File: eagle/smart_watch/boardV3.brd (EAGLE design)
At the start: 100 x 80.3 mm, 62 parts, among them U1 MCP73831, U2 TPS61200, U3 MAX1704X, U4 V_REG_LDOSMD, Y1 16MHz

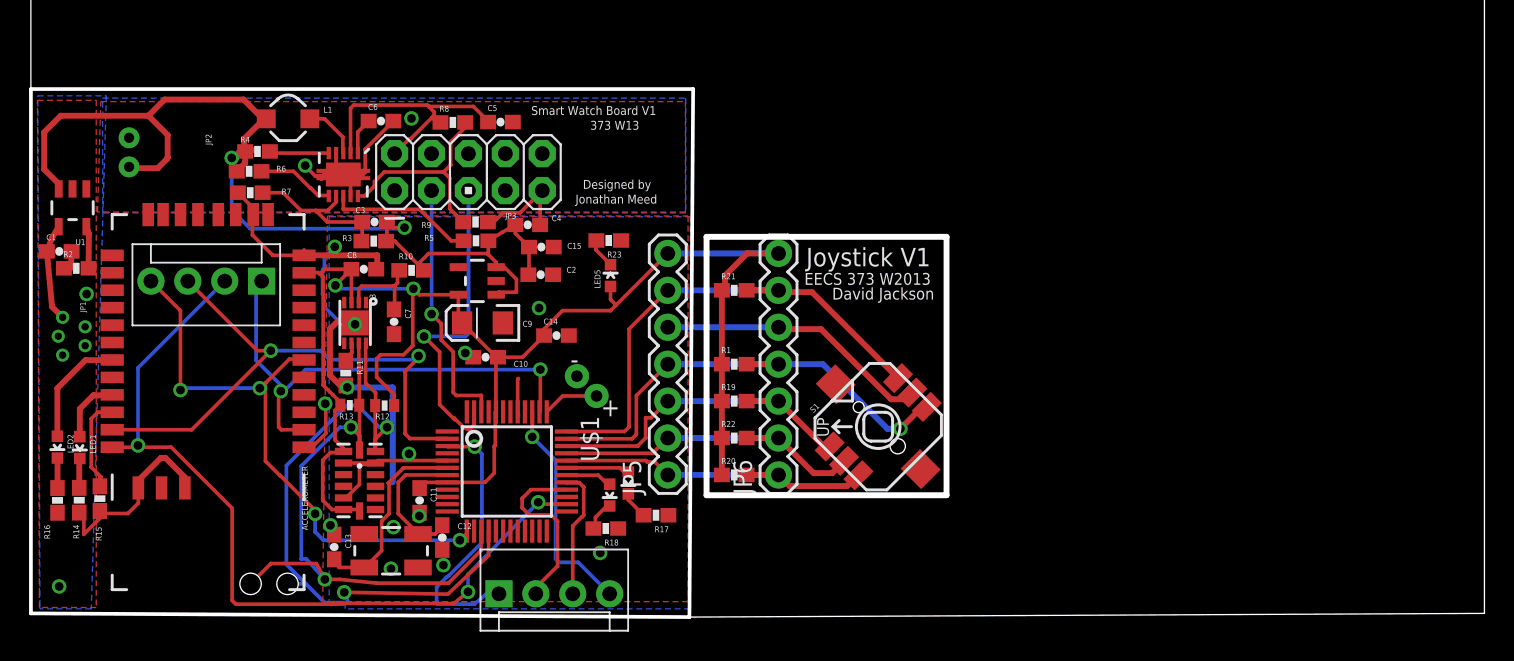
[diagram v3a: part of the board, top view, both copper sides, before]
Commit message: Updated board based on Sam's recs
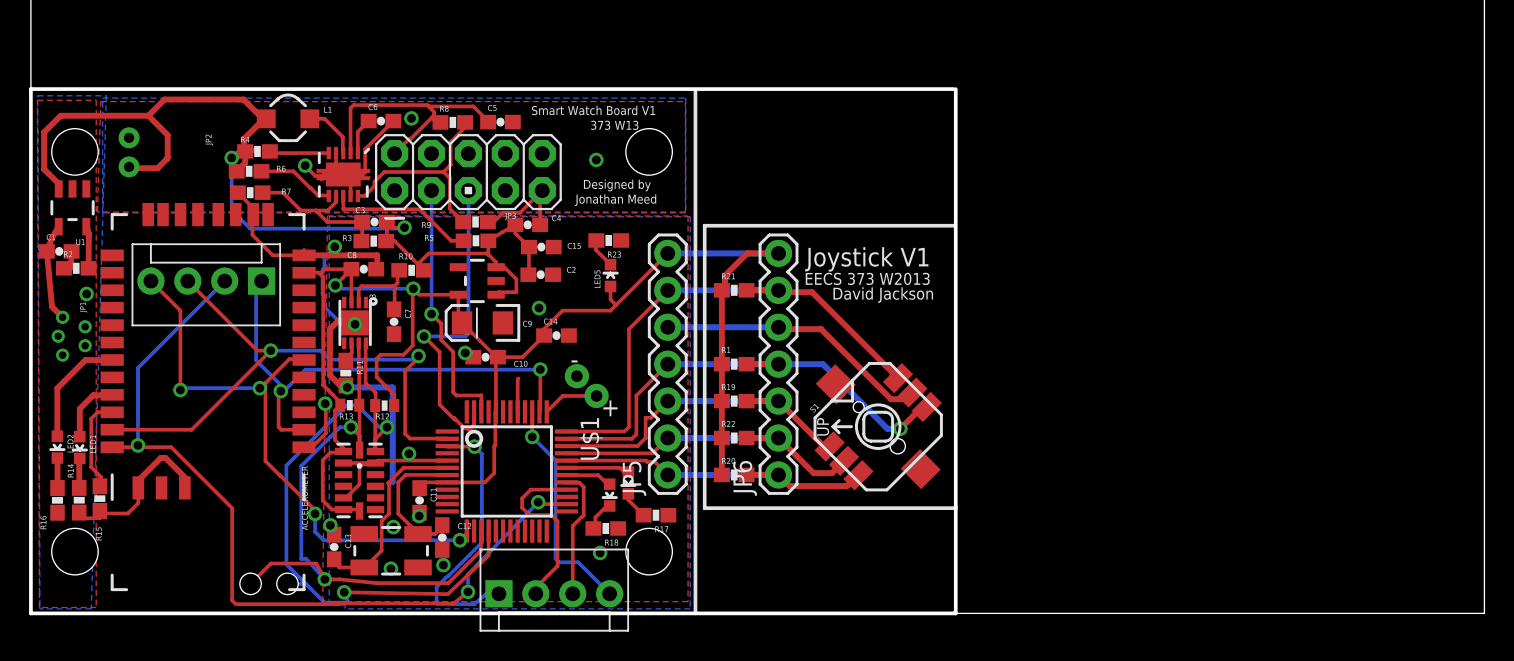
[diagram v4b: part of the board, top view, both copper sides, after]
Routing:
- net GND: track 110.6 -> 109.7 mm
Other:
- board size 100 x 80.3 mm -> 100 x 80 mm
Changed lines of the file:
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@@
 <layer number="42" name="bRestrict" color="1" fill="10" visible="no" active="yes"/>
 <layer number="43" name="vRestrict" color="2" fill="10" visible="no" active="yes"/>
-<layer number="44" name="Drills" color="7" fill="1" visible="no" active="yes"/>
-<layer number="45" name="Holes" color="7" fill="1" visible="no" active="yes"/>
+<layer number="44" name="Drills" color="7" fill="1" visible="yes" active="yes"/>
+<layer number="45" name="Holes" color="7" fill="1" visible="yes" active="yes"/>
 <layer number="46" name="Milling" color="3" fill="1" visible="no" active="yes"/>
 <layer number="47" name="Measures" color="7" fill="1" visible="no" active="yes"/>
@@
 <board>
 <plain>
-<wire x1="45.306" y1="-0.254" x2="100" y2="0" width="0" layer="20"/>
+<wire x1="63.467" y1="0" x2="63.5" y2="0" width="0" layer="20"/>
+<wire x1="63.5" y1="0" x2="100" y2="0" width="0" layer="20"/>
 <wire x1="100" y1="0" x2="100" y2="80" width="0" layer="20"/>
 <wire x1="100" y1="80" x2="0" y2="80" width="0" layer="20"/>
 <wire x1="0" y1="80" x2="0" y2="36.073615625" width="0" layer="20"/>
 <wire x1="0" y1="0" x2="0" y2="36.073615625" width="0.254" layer="20"/>
-<wire x1="45.306" y1="-0.254" x2="45.56" y2="36.073615625" width="0.254" layer="20"/>
-<wire x1="0" y1="0" x2="45.306" y2="-0.254" width="0.254" layer="20"/>
-<wire x1="0" y1="36.073615625" x2="45.56" y2="36.073615625" width="0.254" layer="20"/>
+<wire x1="0" y1="0" x2="63.467" y2="0" width="0.254" layer="20"/>
+<wire x1="0" y1="36.073615625" x2="63.467" y2="36.073615625" width="0.254" layer="20"/>
 <circle x="30.1" y="30.36" radius="1.27" width="0.254" layer="19"/>
-<circle x="3.03" y="4.25" radius="1.6" width="0.1" layer="44"/>
-<circle x="42.53" y="31.75" radius="1.6" width="0.1" layer="44"/>
-<circle x="42.53" y="31.75" radius="1.6" width="0.1" layer="44"/>
-<circle x="42.53" y="4.25" radius="1.5" width="0.254" layer="44"/>
-<circle x="3.03" y="31.75" radius="1.6" width="0.1" layer="44"/>
 <text x="34.417" y="34.29" size="0.6096" layer="25" font="vector">Smart Watch Board V1</text>
 <text x="38.481" y="33.274" size="0.6096" layer="25" font="vector">373 W13</text>
 <text x="37.973" y="29.21" size="0.6096" layer="25" font="vector">Designed by</text>
 <text x="37.465" y="28.194" size="0.6096" layer="25" font="vector">Jonathan Meed</text>
-<wire x1="46.482" y1="8.128" x2="46.482" y2="25.908" width="0.4064" layer="20"/>
-<wire x1="46.482" y1="25.908" x2="62.992" y2="25.908" width="0.4064" layer="20"/>
-<wire x1="62.992" y1="25.908" x2="62.992" y2="8.128" width="0.4064" layer="20"/>
-<wire x1="62.992" y1="8.128" x2="46.482" y2="8.128" width="0.4064" layer="20"/>
 <text x="53.34" y="23.876" size="1.27" layer="25">Joystick V1</text>
 <text x="53.213" y="22.606" size="0.8128" layer="25">EECS 373 W2013</text>
 <text x="55.118" y="21.59" size="0.8128" layer="25">David Jackson</text>
+<wire x1="63.5" y1="0" x2="63.627" y2="0" width="0.254" layer="20"/>
+<wire x1="63.627" y1="0" x2="63.627" y2="36.068" width="0.254" layer="20"/>
+<wire x1="63.5" y1="26.67" x2="46.355" y2="26.67" width="0.254" layer="25"/>
+<wire x1="46.355" y1="26.67" x2="46.355" y2="7.239" width="0.254" layer="25"/>
+<wire x1="46.355" y1="7.239" x2="63.627" y2="7.239" width="0.254" layer="25"/>
+<wire x1="63.627" y1="7.239" x2="63.627" y2="7.366" width="0.254" layer="25"/>
+<wire x1="45.72" y1="35.941" x2="45.72" y2="0" width="0.254" layer="25"/>
+<hole x="42.53" y="31.75" drill="3.2"/>
+<hole x="3.03" y="31.75" drill="3.2"/>
+<hole x="3.03" y="4.25" drill="3.2"/>
+<hole x="42.53" y="4.25" drill="3.2"/>
 </plain>
 <attributes>
@@
 </element>
 <element name="R14" library="SparkFun-Passives" package="0603-RES" value="330" x="3.32566875" y="7.78556875" smashed="yes" rot="R90">
-<attribute name="NAME" x="3.32566875" y="5.11856875" size="0.4064" layer="25" font="vector" rot="R90"/>
-<attribute name="VALUE" x="3.83366875" y="4.99156875" size="0.4064" layer="27" font="vector" rot="R90"/>
+<attribute name="NAME" x="2.94466875" y="9.30956875" size="0.4064" layer="25" font="vector" rot="R90"/>
+<attribute name="VALUE" x="3.83366875" y="9.30956875" size="0.4064" layer="27" font="vector" rot="R90"/>
 </element>
 <element name="R15" library="SparkFun-Passives" package="0603-RES" value="10k" x="4.74328125" y="7.896846875" smashed="yes" rot="R90">
@@
 </element>
 <element name="R16" library="SparkFun-Passives" package="0603-RES" value="330" x="1.83018125" y="7.774071875" smashed="yes" rot="R90">
-<attribute name="NAME" x="1.32218125" y="5.107071875" size="0.4064" layer="25" font="vector" rot="R90"/>
-<attribute name="VALUE" x="2.08418125" y="5.234071875" size="0.4064" layer="27" font="vector" rot="R90"/>
+<attribute name="NAME" x="1.06818125" y="5.742071875" size="0.4064" layer="25" font="vector" rot="R90"/>
+<attribute name="VALUE" x="1.57618125" y="5.234071875" size="0.4064" layer="27" font="vector" rot="R90"/>
 </element>
 <element name="LED3" library="SparkFun-LED" package="LED-0603" value="" x="41.103421875" y="8.970475" smashed="yes" rot="R180">
@@
 </polygon>
 <wire x1="3.436734375" y1="7.024503125" x2="3.32566875" y2="6.93556875" width="0.4064" layer="1"/>
-<via x="1.9412375" y="1.856378125" extent="1-16" drill="0.6"/>
+<via x="38.8982375" y="31.193378125" extent="1-16" drill="0.6"/>
 <wire x1="2.797775" y1="24.904134375" x2="2.7514625" y2="23.78049375" width="0.4064" layer="1"/>
 <wire x1="2.7514625" y1="23.78049375" x2="2.269103125" y2="23.739640625" width="0.4064" layer="1"/>
@@
 <wire x1="4.917796875" y1="6.87233125" x2="4.74328125" y2="7.046846875" width="0.254" layer="1"/>
 <wire x1="4.74328125" y1="7.046846875" x2="4.74328125" y2="6.543925" width="0.254" layer="1"/>
-<wire x1="4.74328125" y1="6.543925" x2="3.644525" y2="5.44516875" width="0.254" layer="1"/>
-<wire x1="3.644525" y1="5.44516875" x2="3.644525" y2="6.6167125" width="0.254" layer="1"/>
 <wire x1="3.644525" y1="6.6167125" x2="3.32566875" y2="6.93556875" width="0.254" layer="1"/>
 <via x="20.24741875" y="14.427375" extent="1-16" drill="0.6"/>
@@
 <wire x1="21.1455" y1="20.1295" x2="22.160646875" y2="20.1295" width="0.4064" layer="1"/>
 <wire x1="22.160646875" y1="20.1295" x2="22.305275" y2="19.984871875" width="0.4064" layer="1"/>
+<wire x1="4.74328125" y1="6.543925" x2="3.32566875" y2="6.543925" width="0.254" layer="1"/>
+<wire x1="3.32566875" y1="6.543925" x2="3.32566875" y2="6.93556875" width="0.254" layer="1"/>
+<wire x1="39.16324375" y1="4.160065625" x2="40.40091875" y2="5.838684375" width="0" layer="19" extent="1-1"/>
 </signal>
 <signal name="N$2">
@@
 </signal>
 </signals>
-<errors>
-</errors>
 </board>
 </drawing>

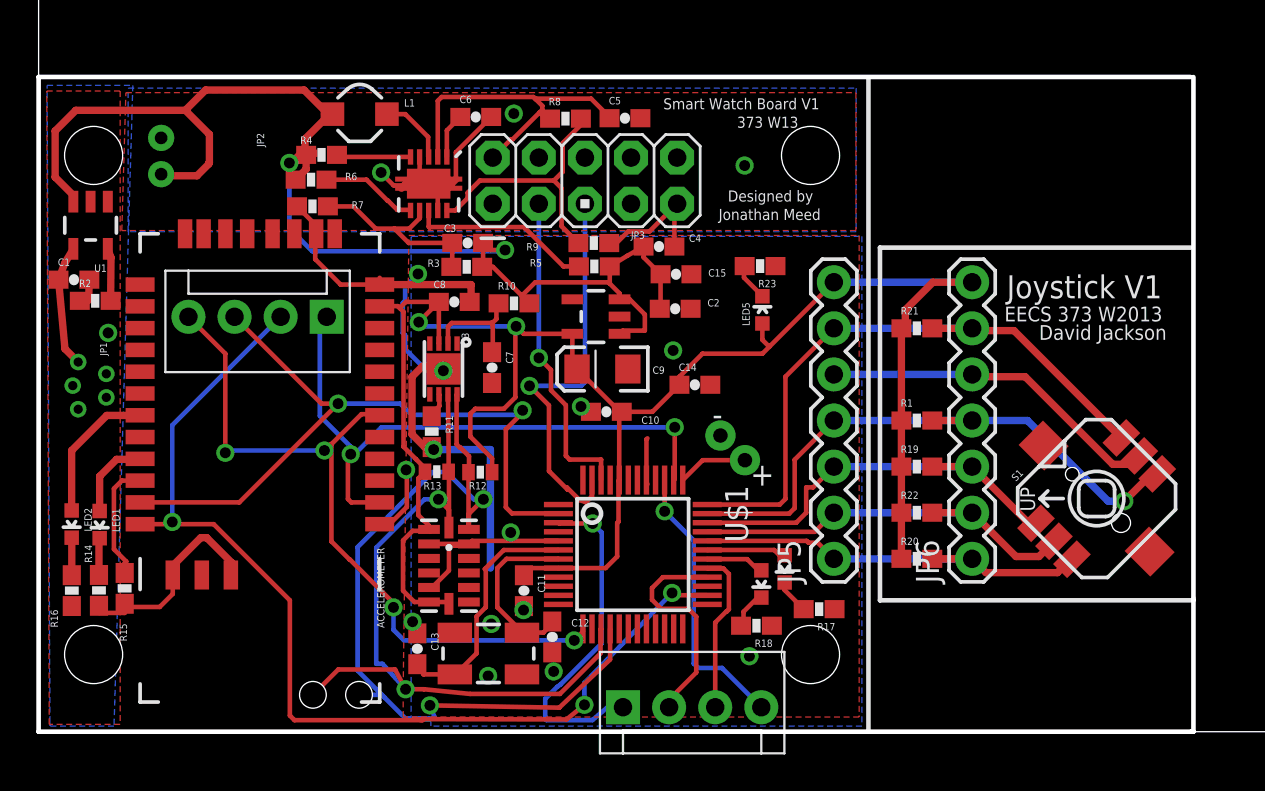
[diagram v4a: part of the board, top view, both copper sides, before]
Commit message: Updated usb port and changed some res sizes
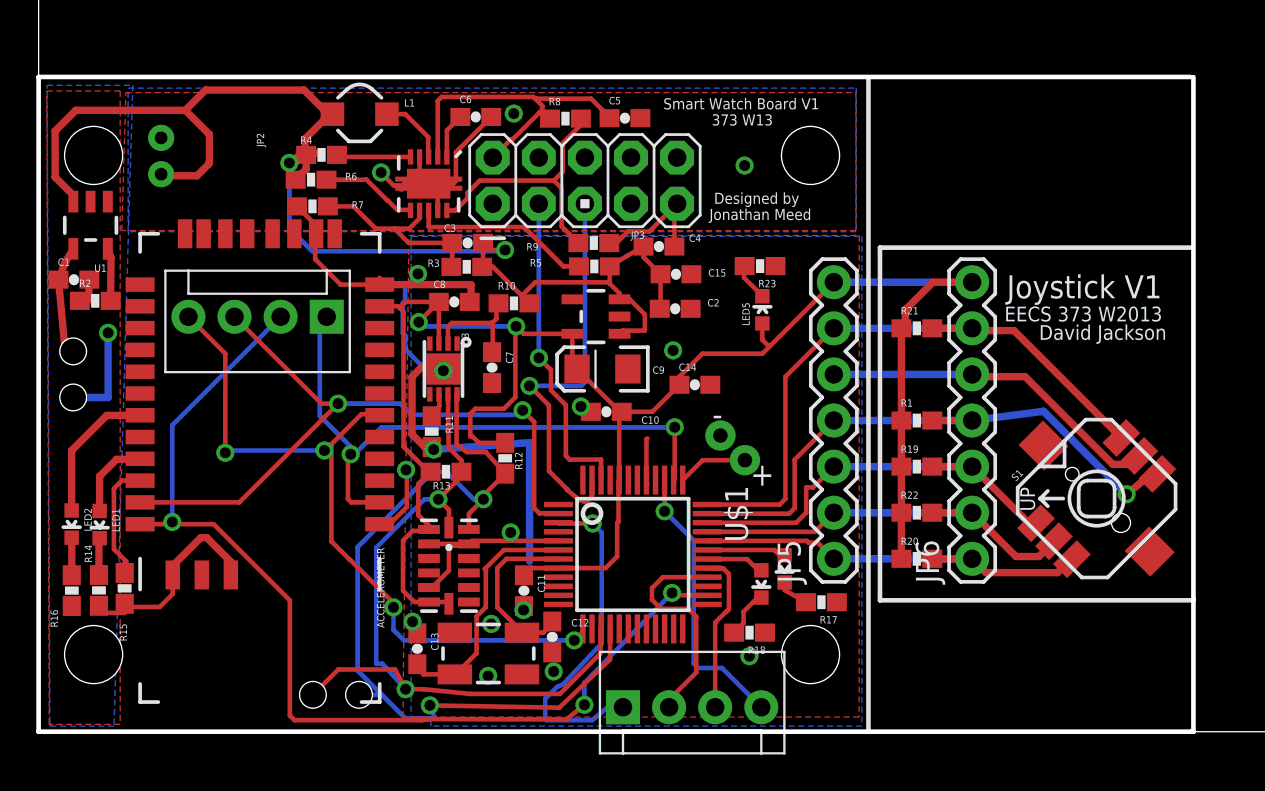
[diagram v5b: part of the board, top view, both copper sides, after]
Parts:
- removed JP1: USB_MICROB_PLUG-PTH, SparkFun-Connectors:MICRO-B-RA-TH
- added RECHARGE: (no value), SparkFun-Connectors:1X02_PP_HOLES_ONLY
- R12, R13: device SparkFun-Passives:0402-RES -> SparkFun-Resistors:0603-RES
- moved R12 1.57 mm to (25.7, 15.1), turned to 90 degrees
- moved R18 0.54 mm to (39.2, 5.46)
- moved R13 0.51 mm to (22.4, 14.3)
- moved R17 0.40 mm to (43.1, 7.13)
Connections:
- net GND: now also RECHARGE.2; no longer JP1.5
- net VBUS: now also RECHARGE.1; no longer JP1.1
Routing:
- net GND: track 109.7 -> 117.4 mm
- net SSEL1: track 40.1 -> 38.6 mm
- net SCL: track 41.7 -> 40.9 mm
- net N$18: track 2.13 -> 2.67 mm
- net VBUS: track 6.75 -> 6.23 mm
